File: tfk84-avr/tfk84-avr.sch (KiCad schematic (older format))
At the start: 34 parts, among them J1 USB_C_Receptacle_USB2.0, J2 AVR-ISP-6, SW1 Reset, U1 ATmega32U4-AU, Y1 16MHz

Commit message: Begin placing mounting holes
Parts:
- H1: footprint MountingHole:MountingHole_2.5mm_Pad_TopOnly -> random-keyboard-parts:MountingHole_2.5mm_Pad_TopOnly_NoCrtYd
- H10, H11, H3, H4, H9: footprint MountingHole:MountingHole_2.5mm_Pad_TopOnly -> random-keyboard-parts:MountingHole_4.5x2.5mm_Pad_TopOnly_NPTH
- H2: value MountingHole -> Case; footprint MountingHole:MountingHole_2.5mm_Pad_TopOnly -> random-keyboard-parts:MountingHole_2.5mm_Pad_TopOnly_NoCrtYd; symbol Mechanical:MountingHole -> Mechanical:MountingHole_Pad
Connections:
- net at D3.2 (A), H1.1: now also H2.1
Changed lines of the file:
@@
 	700  7550 700  5750
 Wire Wire Line
-	1400 6100 1200 6100
+	1400 6100 1300 6100
 $Comp
 L Mechanical:MountingHole_Pad H1
@@
 AR Path="/60815FFC/60989184" Ref="H?"  Part="1"
 F 0 "H1" V 1100 6300 50  0000 C CNN
-F 1 "Case" V 1000 6300 50  0000 C CNN
-F 2 "MountingHole:MountingHole_2.5mm_Pad_TopOnly" H 1100 6100 50  0001 C CNN
+F 1 "Case" V 1000 6300 50  0001 C CNN
+F 2 "random-keyboard-parts:MountingHole_2.5mm_Pad_TopOnly_NoCrtYd" H 1100 6100 50  0001 C CNN
 F 3 "~" H 1100 6100 50  0001 C CNN
 	1    1100 6100
@@
 	3000 1250 2400 1250
 $Comp
-L Mechanical:MountingHole H2
+L Mechanical:MountingHole_Pad H2
 U 1 1 60BC9C45
-P 1050 6300
-F 0 "H2" H 850 6300 50  0000 L CNN
-F 1 "MountingHole" H 950 6050 50  0001 L CNN
-F 2 "MountingHole:MountingHole_2.5mm_Pad_TopOnly" H 1050 6300 50  0001 C CNN
-F 3 "~" H 1050 6300 50  0001 C CNN
-	1    1050 6300
-	1    0    0    -1
+P 1100 6300
+F 0 "H2" V 1100 6450 50  0000 L CNN
+F 1 "Case" V 1000 6400 50  0001 L CNN
+F 2 "random-keyboard-parts:MountingHole_2.5mm_Pad_TopOnly_NoCrtYd" H 1100 6300 50  0001 C CNN
+F 3 "~" H 1100 6300 50  0001 C CNN
+	1    1100 6300
+	0    -1   -1   0
 $EndComp
 $Comp
@@
 F 0 "H3" H 850 6500 50  0000 L CNN
 F 1 "MountingHole" H 1150 6455 50  0001 L CNN
-F 2 "MountingHole:MountingHole_2.5mm_Pad_TopOnly" H 1050 6500 50  0001 C CNN
+F 2 "random-keyboard-parts:MountingHole_4.5x2.5mm_Pad_TopOnly_NPTH" H 1050 6500 50  0001 C CNN
 F 3 "~" H 1050 6500 50  0001 C CNN
 	1    1050 6500
@@
 F 0 "H4" H 850 6700 50  0000 L CNN
 F 1 "MountingHole" H 1150 6655 50  0001 L CNN
-F 2 "MountingHole:MountingHole_2.5mm_Pad_TopOnly" H 1050 6700 50  0001 C CNN
+F 2 "random-keyboard-parts:MountingHole_4.5x2.5mm_Pad_TopOnly_NPTH" H 1050 6700 50  0001 C CNN
 F 3 "~" H 1050 6700 50  0001 C CNN
 	1    1050 6700
@@
 F 0 "H9" H 850 6900 50  0000 L CNN
 F 1 "MountingHole" H 1150 6855 50  0001 L CNN
-F 2 "MountingHole:MountingHole_2.5mm_Pad_TopOnly" H 1050 6900 50  0001 C CNN
+F 2 "random-keyboard-parts:MountingHole_4.5x2.5mm_Pad_TopOnly_NPTH" H 1050 6900 50  0001 C CNN
 F 3 "~" H 1050 6900 50  0001 C CNN
 	1    1050 6900
@@
 F 0 "H10" H 800 7100 50  0000 L CNN
 F 1 "MountingHole" H 1150 7055 50  0001 L CNN
-F 2 "MountingHole:MountingHole_2.5mm_Pad_TopOnly" H 1050 7100 50  0001 C CNN
+F 2 "random-keyboard-parts:MountingHole_4.5x2.5mm_Pad_TopOnly_NPTH" H 1050 7100 50  0001 C CNN
 F 3 "~" H 1050 7100 50  0001 C CNN
 	1    1050 7100
@@
 F 0 "H11" H 800 7300 50  0000 L CNN
 F 1 "MountingHole" H 1150 7255 50  0001 L CNN
-F 2 "MountingHole:MountingHole_2.5mm_Pad_TopOnly" H 1050 7300 50  0001 C CNN
+F 2 "random-keyboard-parts:MountingHole_4.5x2.5mm_Pad_TopOnly_NPTH" H 1050 7300 50  0001 C CNN
 F 3 "~" H 1050 7300 50  0001 C CNN
 	1    1050 7300
 	1    0    0    -1
 $EndComp
+Wire Wire Line
+	1200 6300 1300 6300
+Wire Wire Line
+	1300 6300 1300 6100
+Connection ~ 1300 6100
+Wire Wire Line
+	1300 6100 1200 6100
 $EndSCHEMATC

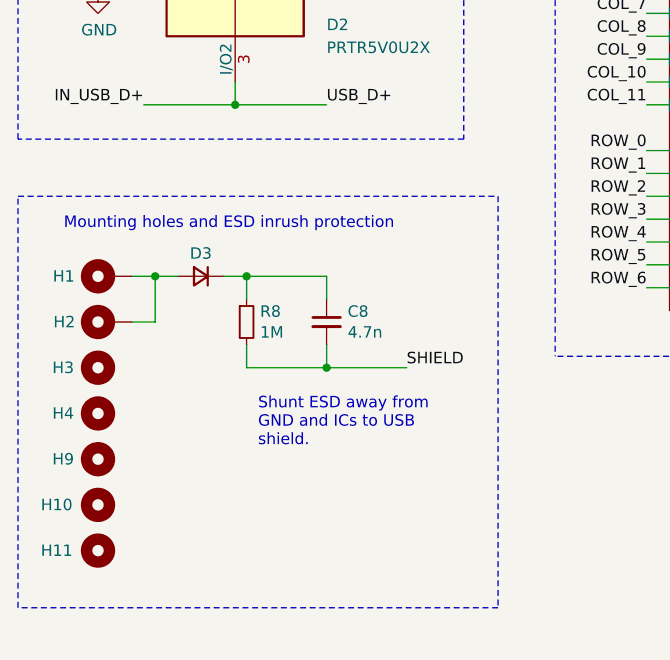
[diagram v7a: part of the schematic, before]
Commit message: Add mounting holes for XD84 and KBD75V2 cases
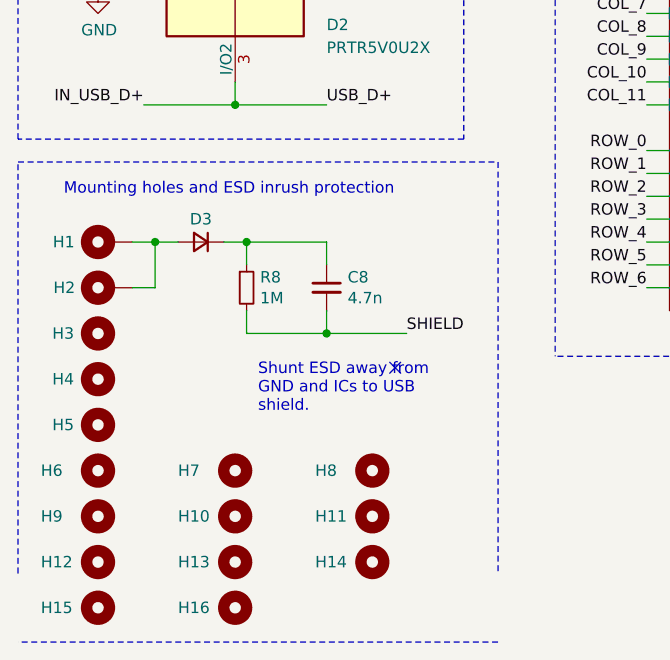
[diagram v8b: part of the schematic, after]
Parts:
- added H10, H11, H12, H13, H14, H15, H16, H7, H8: MountingHole, random-keyboard-parts:MountingHole_4.5x2.5mm_Pad_TopOnly_NPTH, symbol Mechanical:MountingHole
- renumbered H9 to H5, H10 to H6, H11 to H9
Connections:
- no-connect marks 3 -> 4
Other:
- moved on the sheet: C8, D3, H1, H2, H3, H4, H5, H6, H9, R8
